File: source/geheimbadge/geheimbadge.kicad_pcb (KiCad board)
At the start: 2 copper layers, 75.9 x 74.5 mm, 115 parts, among them J1 SAOv2

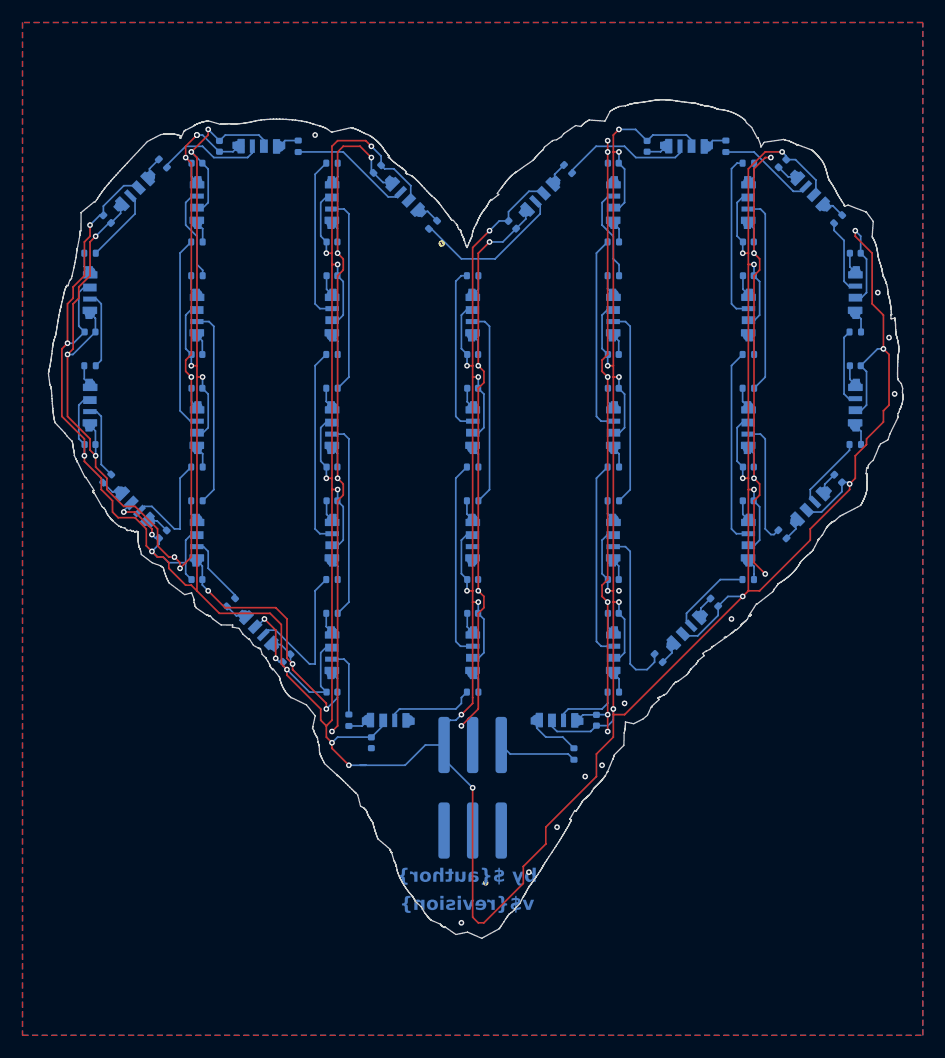
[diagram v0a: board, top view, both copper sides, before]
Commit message: new led orientation; no signal resistors
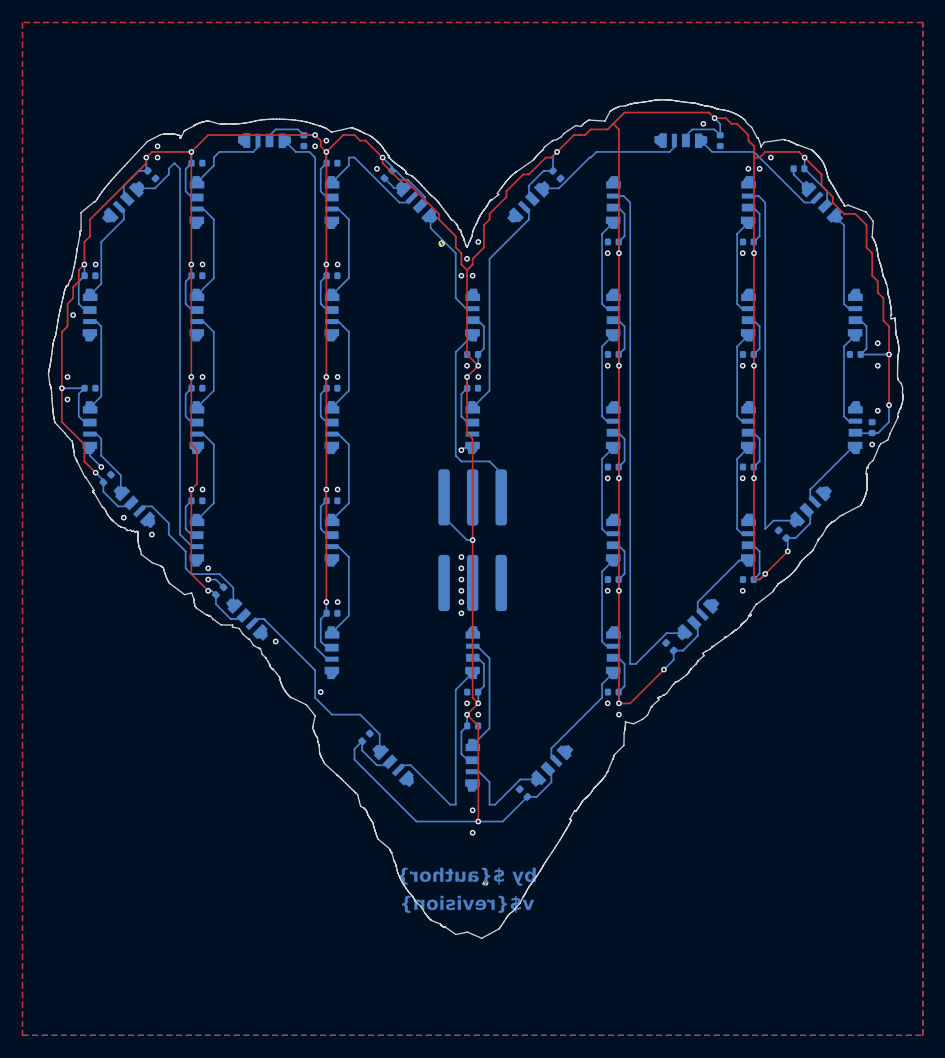
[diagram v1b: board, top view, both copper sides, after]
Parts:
- removed R1, R10, R11, R12, R13, R14, R15, R16, R17, R18, R19, R2, R20, R21, R22, R23, R24, R25, R26, R27, R28, R29, R3, R30, R31, R32, R33, R34, R35, R36, R37, R38, R4, R5, R6, R7, R8, R9: 100, Resistor_SMD:R_0402_1005Metric
- moved C14 68.0 mm to (66.0, 102.5), turned to 0 degrees
- moved D14 68.0 mm to (66.0, 106.0), turned to -90 degrees
- moved D13 67.4 mm to (69.0, 96.0), turned to -135 degrees
- moved D15 67.4 mm to (66.0, 116.0), turned to -90 degrees
- moved C13 64.8 mm to (71.5, 93.5), turned to -45 degrees
- moved C15 64.7 mm to (66.0, 112.5), turned to 0 degrees
- moved D20 59.2 mm to (100.0, 146.0), turned to -90 degrees
- moved D21 58.7 mm to (107.0, 146.0), turned to 45 degrees
- moved D16 58.5 mm to (70.0, 123.0), turned to -45 degrees
- moved C12 57.0 mm to (75.5, 122.5), turned to 0 degrees
- moved C16 56.3 mm to (67.5, 120.5), turned to 45 degrees
- moved C21 56.2 mm to (104.5, 148.5), turned to 135 degrees
- moved D8 55.8 mm to (81.5, 90.5), turned to 180 degrees
- moved C20 55.5 mm to (100.0, 142.5), turned to 0 degrees
- moved C34 55.1 mm to (134.0, 109.5), turned to 180 degrees
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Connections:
- D1 pad 1: Net-(D1-DIN) -> /GPIO1
- D10 pad 1: Net-(D10-DIN) -> /pixel8/D_{out}
- D11 pad 1: Net-(D11-DIN) -> /pixel10/D_{in}
- D12 pad 1: Net-(D12-DIN) -> /pixel10/D_{out}
- D13 pad 1: Net-(D13-DIN) -> /pixel11/D_{out}
- D14 pad 1: Net-(D14-DIN) -> /pixel12/D_{out}
- D15 pad 1: Net-(D15-DIN) -> /pixel13/D_{out}
- D16 pad 1: Net-(D16-DIN) -> /pixel14/D_{out}
- D17 pad 1: Net-(D17-DIN) -> /pixel15/D_{out}
- D18 pad 1: Net-(D18-DIN) -> /pixel16/D_{out}
- D19 pad 1: Net-(D19-DIN) -> /pixel17/D_{out}
- D2 pad 1: Net-(D2-DIN) -> /pixel0/D_{out}
- D20 pad 1: Net-(D20-DIN) -> /pixel18/D_{out}
- D21 pad 1: Net-(D21-DIN) -> /pixel19/D_{out}
- D22 pad 1: Net-(D22-DIN) -> /pixel20/D_{out}
- D23 pad 1: Net-(D23-DIN) -> /pixel21/D_{out}
- D24 pad 1: Net-(D24-DIN) -> /pixel22/D_{out}
- D25 pad 1: Net-(D25-DIN) -> /pixel23/D_{out}
- D26 pad 1: Net-(D26-DIN) -> /pixel24/D_{out}
- D27 pad 1: Net-(D27-DIN) -> /pixel25/D_{out}
- D28 pad 1: Net-(D28-DIN) -> /pixel26/D_{out}
- D29 pad 1: Net-(D29-DIN) -> /pixel27/D_{out}
- D3 pad 1: Net-(D3-DIN) -> /pixel1/D_{out}
- D30 pad 1: Net-(D30-DIN) -> /pixel28/D_{out}
- D31 pad 1: Net-(D31-DIN) -> /pixel29/D_{out}
- D32 pad 1: Net-(D32-DIN) -> /pixel30/D_{out}
- D33 pad 1: Net-(D33-DIN) -> /pixel31/D_{out}
- D33 pad 3: /pixel33/D_{out} -> /pixel32/D_{out}
- D34 pad 1: Net-(D34-DIN) -> /pixel32/D_{out}
- D34 pad 3: /pixel34/D_{out} -> /pixel33/D_{out}
- D35 pad 1: Net-(D35-DIN) -> /pixel33/D_{out}
- D35 pad 3: /pixel35/D_{out} -> /pixel34/D_{out}
- D36 pad 1: Net-(D36-DIN) -> /pixel34/D_{out}
- D36 pad 3: /pixel36/D_{out} -> /pixel35/D_{out}
- D37 pad 1: Net-(D37-DIN) -> /pixel35/D_{out}
- D37 pad 3: /pixel37/D_{out} -> /pixel36/D_{out}
- D38 pad 1: Net-(D38-DIN) -> /pixel36/D_{out}
- D38 pad 3: /pixel38/D_{out} -> /pixel37/D_{out}
- D4 pad 1: Net-(D4-DIN) -> /pixel2/D_{out}
- D5 pad 1: Net-(D5-DIN) -> /pixel3/D_{out}
- D6 pad 1: Net-(D6-DIN) -> /pixel4/D_{out}
- D7 pad 1: Net-(D7-DIN) -> /pixel5/D_{out}
- D8 pad 1: Net-(D8-DIN) -> /pixel6/D_{out}
- D9 pad 1: Net-(D9-DIN) -> /pixel7/D_{out}
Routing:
- net GND: track 372.0 -> 9.00 mm, vias 42 -> 58
- net VCC: track 660.9 -> 586.0 mm, vias 43 -> 38
- net /pixel6/D_{out}: track 7.49 -> 48.7 mm
- net /pixel11/D_{out}: track 6.72 -> 39.6 mm
- net /pixel25/D_{out}: track 17.6 -> 48.6 mm
- net /pixel37/D_{out}: track 17.6 -> 0.00 mm
- net /pixel30/D_{out}: track 17.6 -> 33.7 mm
- net /GPIO1: track 7.00 -> 18.2 mm
- net /pixel31/D_{out}: track 17.6 -> 6.79 mm
- net /pixel7/D_{out}: track 17.6 -> 7.71 mm
- net /pixel28/D_{out}: track 17.6 -> 8.80 mm
- net /pixel32/D_{out}: track 0.00 -> 8.80 mm
- net /pixel23/D_{out}: track 17.3 -> 8.80 mm
- net /pixel4/D_{out}: track 17.6 -> 9.21 mm
- net /pixel2/D_{out}: track 17.6 -> 9.21 mm
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
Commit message: flipped board
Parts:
- C1, C10, C11, C12, C13, C14, C15, C16, C17, C18, C19, C2, C20, C21, C22, C23, C24, C25, C26, C27, C28, C29, C3, C30, C31, C32, C33, C34, C35, C36, C37, C38, C4, C5, C6, C7, C8, C9, D1, D10, D11, D12, D13, D14, D15, D16, D17, D18, D19, D2, D20, D21, D22, D23, D24, D25, D26, D27, D28, D29, D3, D30, D31, D32, D33, D34, D35, D36, D37, D38, D4, D5, D6, D7, D8, D9, J1: moved to F.Cu
- moved C33 71.0 mm to (64.5, 116.0)
- moved C14 68.0 mm to (134.0, 102.5), turned to 180 degrees
- moved C15 68.0 mm to (134.0, 112.5), turned to 180 degrees
- moved C34 68.0 mm to (66.0, 109.5), turned to 0 degrees
- moved D14 68.0 mm to (134.0, 106.0)
- moved D15 68.0 mm to (134.0, 116.0)
- moved D33 68.0 mm to (66.0, 116.0)
- moved D34 68.0 mm to (66.0, 106.0)
- moved C16 64.9 mm to (132.5, 120.5), turned to 135 degrees
- moved D13 62.0 mm to (131.0, 96.0), turned to -45 degrees
- moved D35 62.0 mm to (69.0, 96.0), turned to 45 degrees
- moved D16 60.0 mm to (130.0, 123.0), turned to -135 degrees
- moved D32 60.0 mm to (70.0, 123.0), turned to 135 degrees
- moved C35 58.0 mm to (71.0, 93.0), turned to 0 degrees
- moved C13 57.1 mm to (128.5, 93.5), turned to -135 degrees
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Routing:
- net GND: track 9.00 -> 16.9 mm, vias 58 -> 69
- net /pixel19/D_{out}: track 9.04 -> 14.5 mm
- net /pixel17/D_{out}: track 19.0 -> 24.5 mm
- net /pixel20/D_{out}: track 10.2 -> 12.8 mm
- net VCC: track 586.0 -> 587.4 mm
- net /pixel16/D_{out}: track 18.7 -> 19.8 mm
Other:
- outline, holes or cut-outs redrawn

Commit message: finalized controller design
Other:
- board text added: "0, 3"
- board text added: "10"
- board text added: "11, 16"
- board text added: "12"
- board text added: "13"
- board text added: "14, 15"
- board text added: "17"
- board text added: "20"
- board text added: "22"
- board text added: "23"
- board text added: "24"
- board text added: "25"
- board text added: "26, 27"
- board text added: "28"
- board text added: "29"
- board text added: "30, 35"
- board text added: "32, 31"
- board text added: "33"
- board text added: "34"
- board text added: "4"
- board text added: "5"
- board text added: "6, 18"
- board text added: "7, 8"
- board text added: "9"
- board text removed: "10, 15"
- board text removed: "11, 12, 13"
- board text removed: "14"
- board text removed: "16"
- board text removed: "17, 4"
- board text removed: "18, 31"
- board text removed: "19"
- board text removed: "20, 25"
- board text removed: "22, 23, 24"
- board text removed: "26, 30"
- board text removed: "27, 28, 29"
- board text removed: "3"
- board text removed: "32, 36"
- board text removed: "33, 34, 35"
- board text removed: "37"
- board text removed: "38"
- board text removed: "5, 9"
- board text removed: "6, 7, 8"

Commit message: finalized all designs
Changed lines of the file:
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@@
 	(property "company" "Geheimorganisation")
 	(property "pid" "tba")
-	(property "revision" "0.1.1")
+	(property "revision" "1.0.0")
 	(property "title" "Geheimbadge")
 	(net 0 "")
@@
 		)
 	)
+	(gr_rect
+		(start 101.5 119.5)
+		(end 103.5 125)
+		(stroke
+			(width 0)
+			(type solid)
+		)
+		(fill solid)
+		(layer "F.Cu")
+		(net 1)
+	)
+	(gr_rect
+		(start 96.5 127)
+		(end 98.5 132.5)
+		(stroke
+			(width 0)
+			(type solid)
+		)
+		(fill solid)
+		(layer "F.Cu")
+		(net 6)
+	)
+	(gr_rect
+		(start 99 119.5)
+		(end 101 125)
+		(stroke
+			(width 0)
+			(type solid)
+		)
+		(fill solid)
+		(layer "F.Cu")
+		(net 3)
+	)
+	(gr_rect
+		(start 96.5 119.5)
+		(end 98.5 125)
+		(stroke
+			(width 0)
+			(type solid)
+		)
+		(fill solid)
+		(layer "F.Cu")
+		(net 4)
+	)
+	(gr_rect
+		(start 101.5 127)
+		(end 103.5 132.5)
+		(stroke
+			(width 0)
+			(type solid)
+		)
+		(fill solid)
+		(layer "F.Cu")
+		(net 2)
+	)
 	(gr_poly

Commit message: update pixel idices
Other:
- board text added: "23, 37"
- board text added: "25, 36"
- board text removed: "23"
- board text removed: "25"
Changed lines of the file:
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@@
 		)
 	)
-	(gr_text "25"
+	(gr_text "25, 36"
 		(at 88 100.5 0)
 		(layer "Cmts.User")
@@
 		)
 	)
-	(gr_text "23"
+	(gr_text "23, 37"
 		(at 88 120.5 0)
 		(layer "Cmts.User")
